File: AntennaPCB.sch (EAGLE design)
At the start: 1 part

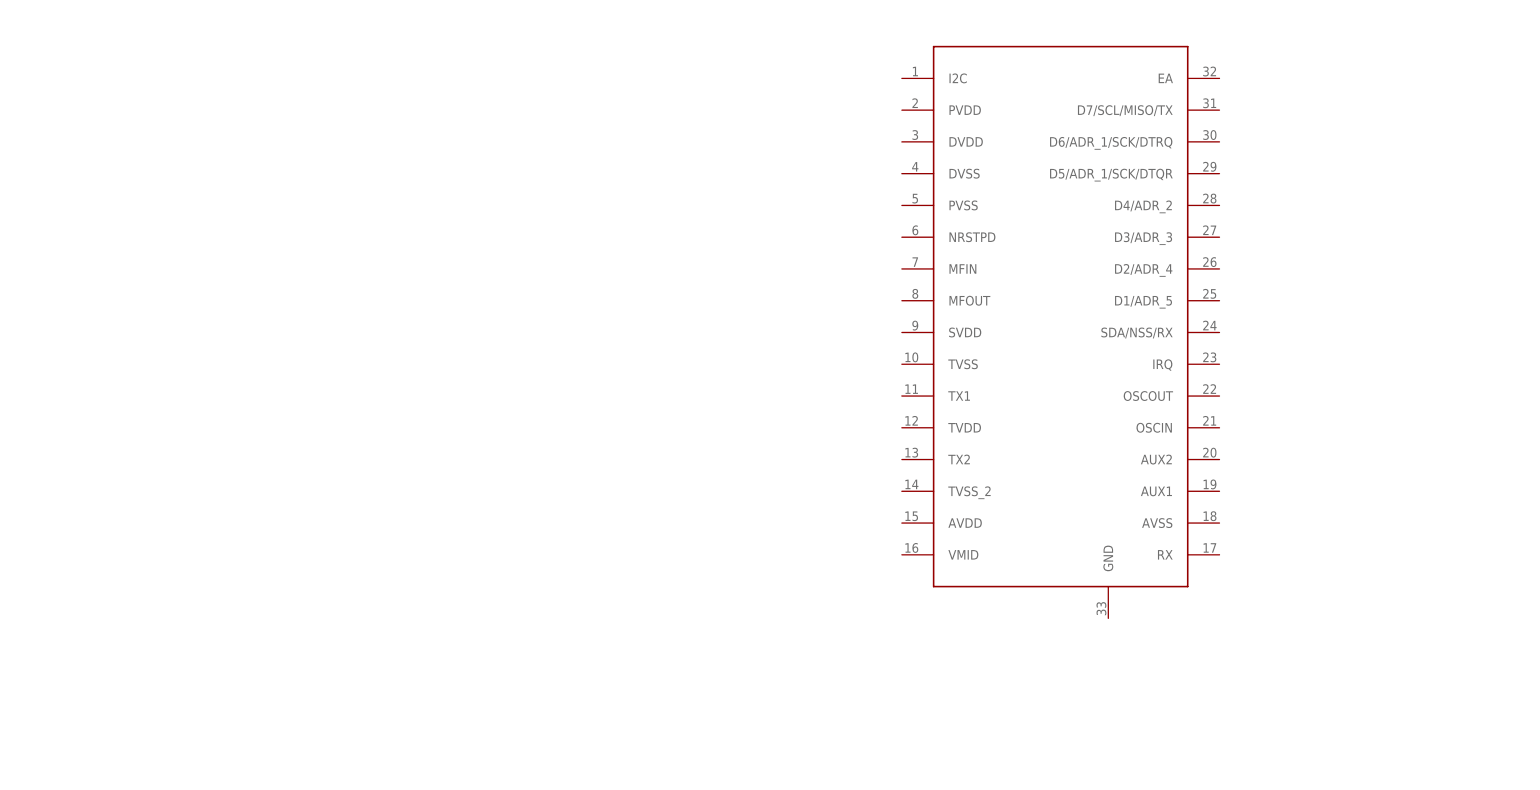
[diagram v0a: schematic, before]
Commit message: updated schematic with RFID reader
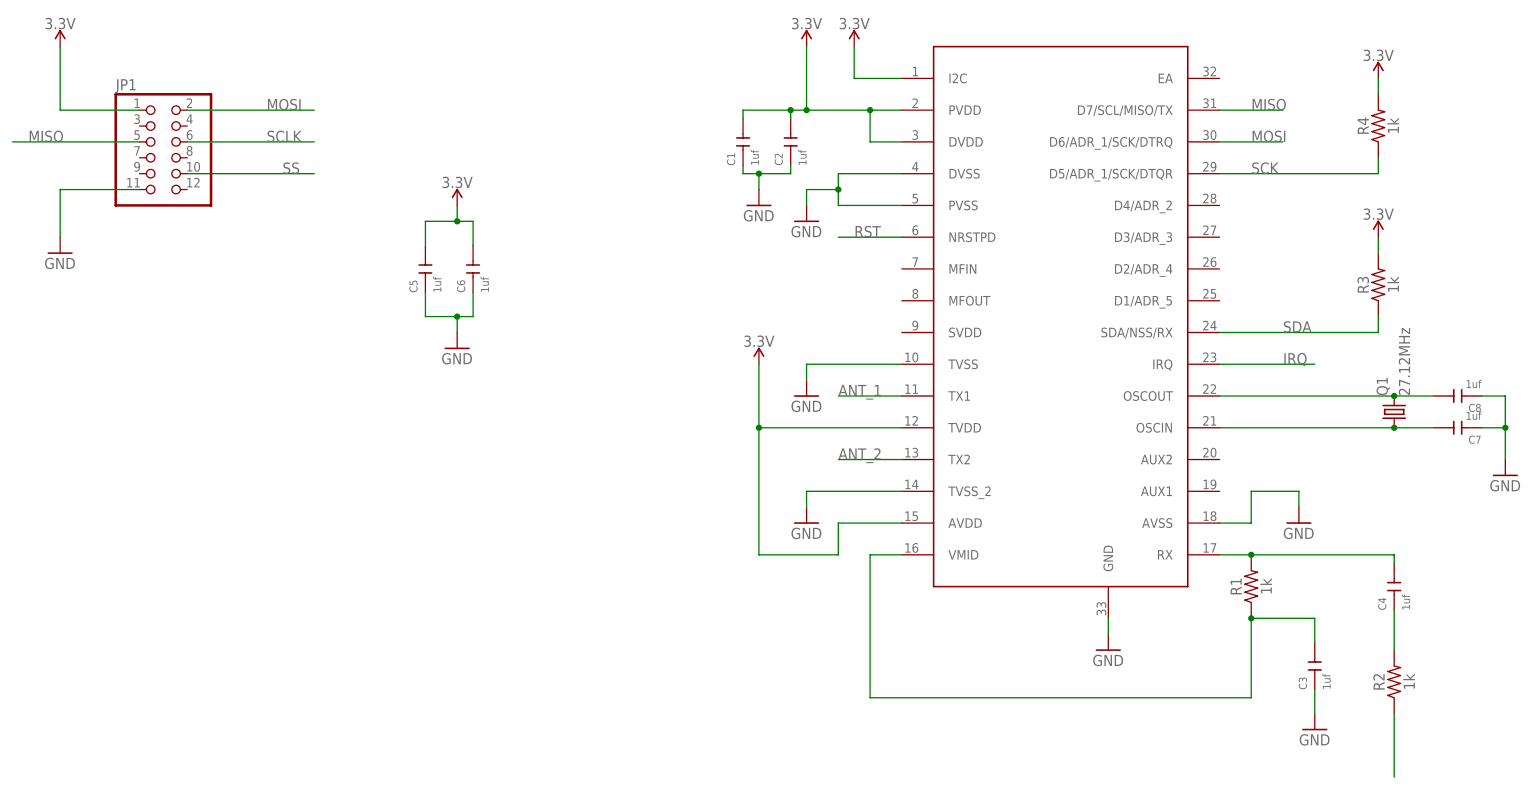
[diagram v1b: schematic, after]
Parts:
- added C1, C2, C3, C4, C5, C6, C7, C8: 1uf, Seeed-Capacitor:CERAMIC-1UF-25V-10%-X7R(0603)
- added JP1: (no value), pinhead:PINHD-2X6
- added Q1: 27.12MHz, crystal:CRYSTALHC49S
- added R1, R2, R3, R4: 1k, SparkFun-Resistors:1KOHM-0603-1/10W-1%
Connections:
- new net 3.3V: C1.2, C2.2, C5.2, C6.2, JP1.1, R3.2, R4.2, U$1.AVDD, U$1.DVDD, U$1.I2C, U$1.PVDD, U$1.TVDD
- new net ANT_1: U$1.TX1
- new net ANT_2: U$1.TX2
- new net GND: C1.1, C2.1, C3.1, C5.1, C6.1, C7.1, C8.1, JP1.11, U$1.AVSS, U$1.DVSS, U$1.GND, U$1.PVSS, U$1.TVSS, U$1.TVSS_2
- new net IRQ: U$1.IRQ
- new net MISO: JP1.5, U$1.D7/SCL/MISO/TX
- new net MOSI: JP1.2, U$1.D6/ADR_1/SCK/DTRQ
- new net N$1: C3.2, R1.1, U$1.VMID
- new net N$2: C4.2, R1.2, U$1.RX
- new net N$3: C4.1, R2.2
- new net N$4: R2.1
- new net N$5: C8.2, Q1.2, U$1.OSCOUT
- new net N$6: C7.2, Q1.1, U$1.OSCIN
- new net RST: U$1.NRSTPD
- new net SCK: R4.1, U$1.D5/ADR_1/SCK/DTQR
- new net SCLK: JP1.6
- new net SDA: R3.1, U$1.SDA/NSS/RX
- new net SS: JP1.10
